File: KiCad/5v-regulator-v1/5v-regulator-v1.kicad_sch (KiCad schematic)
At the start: 43 parts, among them J1 Screw_Terminal_01x02, J2 USB-A1SSW6, J3 USB-A1SSW6, J4 USB-A1SSW6, J5 USB-A1SSW6, J6 Screw_Terminal_01x04, Q1 Q_Dual_NMOS_S1G1D2S2G2D1, SW1 SW_SPST, SW2 SW_SPST, U1 TPS51386RJNR, U2 INA219AIDR, U3 INA219AIDR

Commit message: Blaine review
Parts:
- added J7: Conn_01x04_Pin, Connector_PinHeader_2.54mm:PinHeader_1x04_P2.54mm_Vertical, symbol Connector:Conn_01x04_Pin
- added R11, R12: 10K, Resistor_SMD:R_0805_2012Metric_Pad1.20x1.40mm_HandSolder, symbol Device:R
- J2, J3, J4, J5: footprint Vertical USB:ONSHORE_USB-A1SSW6 -> Connector_USB:USB_A_Wuerth_614004134726_Horizontal; symbol Vertical USB-A:USB-A1SSW6 -> Connector:USB_A
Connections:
- net GND: now also J2.5 (Shield), J3.5 (Shield), J4.5 (Shield), J5.5 (Shield), J6.2 (Pin_2), J7.2 (Pin_2); no longer J2.S1 (SHIELD), J2.S2 (SHIELD__1), J2.S3 (SHIELD__2), J2.S4 (SHIELD__3), J3.S1 (SHIELD), J3.S2 (SHIELD__1), J3.S3 (SHIELD__2), J3.S4 (SHIELD__3), J4.S1 (SHIELD), J4.S2 (SHIELD__1), J4.S3 (SHIELD__2), J4.S4 (SHIELD__3), J5.S1 (SHIELD), J5.S2 (SHIELD__1), J5.S3 (SHIELD__2), J5.S4 (SHIELD__3), J6.3 (Pin_3)
- net VBATT: now also Q1.5 (G), R7.1; no longer U2.8 (VIN+)
- net VIN: no longer U2.7 (VIN-)
- net VOUT: no longer U3.8 (VIN+)
- net VOUT2: now also J6.3 (Pin_3), J7.1 (Pin_1), R11.1, R12.1; no longer J6.2 (Pin_2), U3.7 (VIN-)
- net at U2.2 (A0), U2.3 (SDA), U3.3 (SDA): now also J7.3 (Pin_3), R11.2
- net at U2.4 (SCL), U3.2 (A0), U3.4 (SCL): now also J7.4 (Pin_4), R12.2

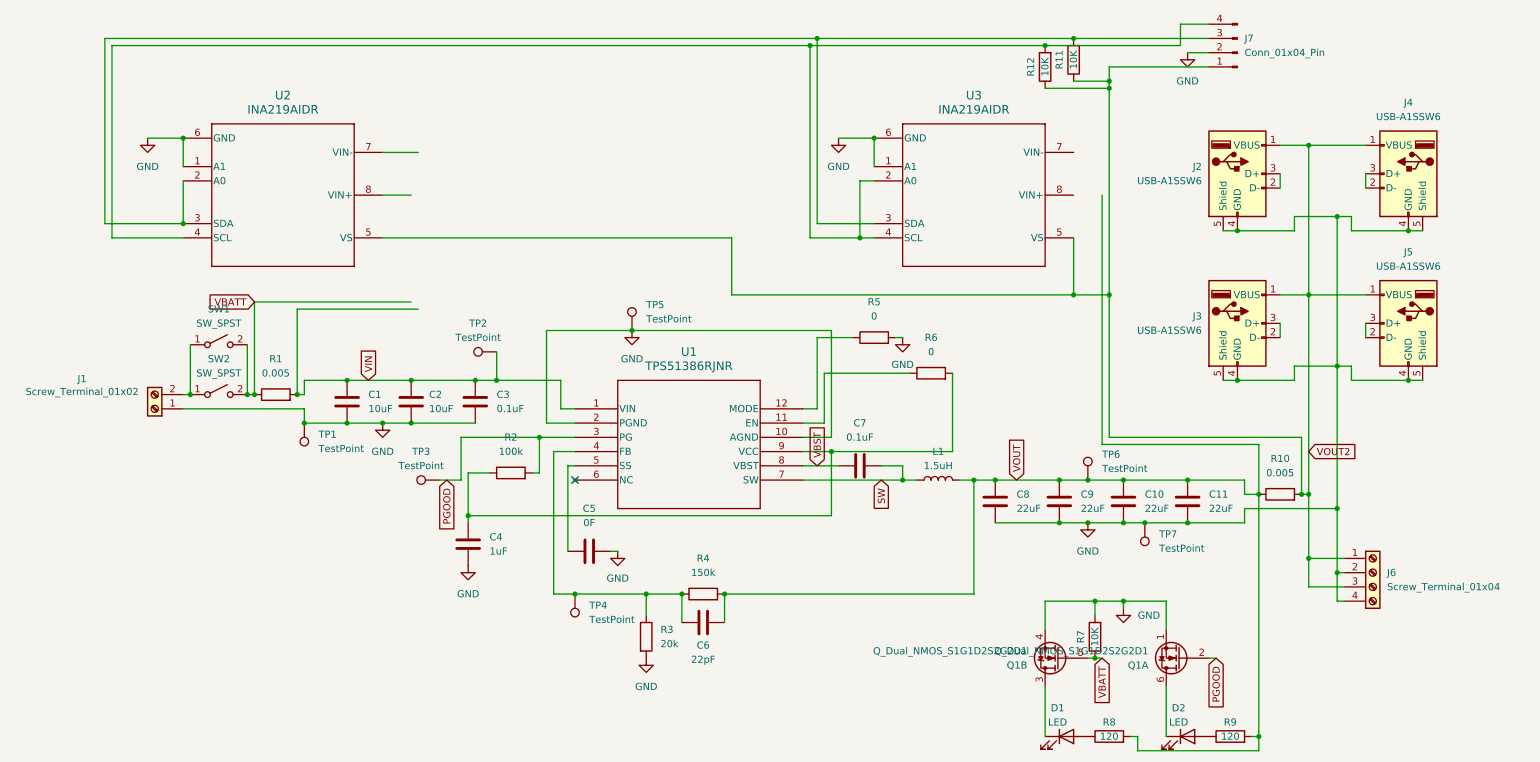
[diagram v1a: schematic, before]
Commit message: Updated 5V reg and added battery meter
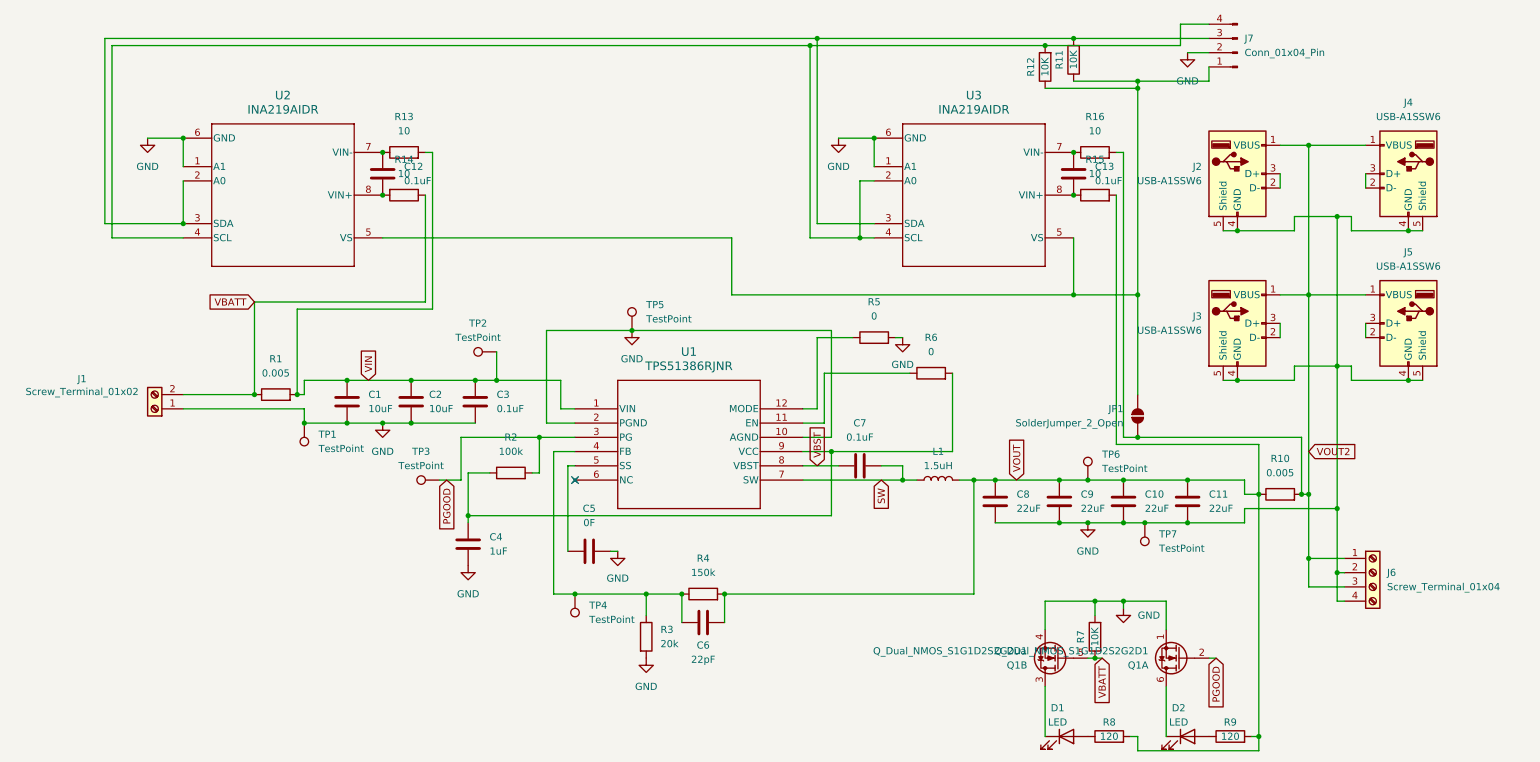
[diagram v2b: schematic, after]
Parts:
- removed SW1: SW_SPST, Connector_PinHeader_2.54mm:PinHeader_1x02_P2.54mm_Vertical, symbol Switch:SW_SPST
- removed SW2: SW_SPST, symbol Switch:SW_SPST
- added C12, C13: 0.1uF, Capacitor_SMD:C_1206_3216Metric_Pad1.33x1.80mm_HandSolder, symbol Device:C
- added JP1: SolderJumper_2_Open, Jumper:SolderJumper-2_P1.3mm_Open_TrianglePad1.0x1.5mm, symbol Jumper:SolderJumper_2_Open
- added R13, R14, R15, R16: 10, Resistor_SMD:R_1206_3216Metric_Pad1.30x1.75mm_HandSolder, symbol Device:R
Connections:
- net VBATT: now also J1.2 (Pin_2), R14.1
- net VIN: now also R13.2
- net VOUT: now also R15.2
- net VOUT2: now also JP1.1 (A), R16.2; no longer J7.1 (Pin_1), R11.1, R12.1, U2.5 (VS), U3.5 (VS)
- net at U2.7 (VIN-): now also C12.1, R13.1
- net at U2.8 (VIN+): now also C12.2, R14.2
- net at U3.7 (VIN-): now also C13.1, R16.1
- net at U3.8 (VIN+): now also C13.2, R15.1
- new net: J7.1 (Pin_1), JP1.2 (B), R11.1, R12.1, U2.5 (VS), U3.5 (VS)

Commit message: Sent to production!
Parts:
- added JP2: Jumper_2_Bridged, TPS51386:usb_symbol, symbol Jumper:Jumper_2_Bridged
- C5, R5, R6: now not fitted
- L1: footprint Wurth_Inductor:IND_WE-LHMI_8030_WRE -> TPS51386:L_Panasonic_ETQP4M---KVK
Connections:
- net at J7.1 (Pin_1), JP1.2 (B), R11.1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: now also JP2.1 (A)
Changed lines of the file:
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@@
 	)
 	(junction
+		(at 130.81 62.23)
+		(diameter 0)
+		(color 0 0 0 0)
+	)
+	(junction
 		(at 72.39 95.25)
 		(diameter 0)
@@
 	(wire
 		(pts
-			(xy 261.62 87.63) (xy 264.16 87.63)
+			(xy 130.81 72.39) (xy 201.93 72.39)
 		)
 		(stroke
@@
 	(wire
 		(pts
-			(xy 241.3 58.42) (xy 248.92 58.42)
+			(xy 261.62 87.63) (xy 264.16 87.63)
 		)
 		(stroke
@@
 	(wire
 		(pts
-			(xy 238.76 72.39) (xy 243.84 72.39)
+			(xy 241.3 58.42) (xy 248.92 58.42)
 		)
 		(stroke
@@
 	(wire
 		(pts
-			(xy 232.41 107.95) (xy 232.41 105.41)
+			(xy 238.76 72.39) (xy 243.84 72.39)
 		)
 		(stroke
@@
 	(wire
 		(pts
-			(xy 238.76 45.72) (xy 243.84 45.72)
+			(xy 232.41 107.95) (xy 232.41 105.41)
 		)
 		(stroke
@@
 	(wire
 		(pts
-			(xy 201.93 34.29) (xy 213.36 34.29)
+			(xy 238.76 45.72) (xy 243.84 45.72)
 		)
 		(stroke
@@
 	(wire
 		(pts
-			(xy 105.41 104.14) (xy 106.68 104.14)
+			(xy 201.93 34.29) (xy 213.36 34.29)
 		)
 		(stroke
@@
 	(wire
 		(pts
-			(xy 78.74 62.23) (xy 140.97 62.23)
+			(xy 105.41 104.14) (xy 106.68 104.14)
 		)
 		(stroke
@@
 	(wire
 		(pts
-			(xy 140.97 72.39) (xy 201.93 72.39)
+			(xy 130.81 72.39) (xy 130.81 62.23)
 		)
 		(stroke
@@
 	(wire
 		(pts
+			(xy 78.74 62.23) (xy 130.81 62.23)
+		)
+		(stroke
+			(width 0)
+			(type default)
+		)
+	)
+	(wire
+		(pts
 			(xy 201.93 62.23) (xy 201.93 72.39)
 		)
@@
 	(wire
 		(pts
-			(xy 140.97 62.23) (xy 140.97 72.39)
-		)
-		(stroke
-			(width 0)
-			(type default)
-		)
-	)
-	(wire
-		(pts
 			(xy 184.15 105.41) (xy 187.96 105.41)
 		)
@@
 	(global_label "VOUT2"
 		(shape input)
-		(at 243.84 100.33 0)
+		(at 243.84 92.71 180)
 		(fields_autoplaced yes)
 		(effects
@@
 				(size 1.27 1.27)
 			)
-			(justify left)
+			(justify right)
 		)
 		(property "Intersheetrefs" "${INTERSHEET_REFS}"
-			(at 252.7519 100.33 0)
+			(at 234.9281 92.71 0)
 			(effects
 				(font
 					(size 1.27 1.27)
 				)
-				(justify left)
+				(justify right)
 				(hide yes)
 			)
@@
 		(in_bom yes)
 		(on_board yes)
-		(dnp no)
+		(dnp yes)
 		(fields_autoplaced yes)
 		(property "Reference" "R5"
@@
 		(in_bom yes)
 		(on_board yes)
-		(dnp no)
+		(dnp yes)
 		(fields_autoplaced yes)
 		(property "Reference" "R6"
@@
 		(in_bom yes)
 		(on_board yes)
-		(dnp no)
+		(dnp yes)
 		(fields_autoplaced yes)
 		(property "Reference" "C5"
@@
 	)
 	(symbol
+		(lib_id "Jumper:Jumper_2_Bridged")
+		(at 135.89 62.23 0)
+		(unit 1)
+		(exclude_from_sim yes)
+		(in_bom yes)
+		(on_board yes)
+		(dnp no)
+		(fields_autoplaced yes)
+		(property "Reference" "JP2"
+			(at 135.89 57.15 0)
+			(effects
+				(font
+					(size 1.27 1.27)
+				)
+			)
+		)
+		(property "Value" "Jumper_2_Bridged"
+			(at 135.89 59.69 0)
+			(effects
+				(font
+					(size 1.27 1.27)
+				)
+			)
+		)
+		(property "Footprint" "TPS51386:usb_symbol"
+			(at 135.89 62.23 0)
+			(effects
+				(font
+					(size 1.27 1.27)
+				)
+				(hide yes)
+			)
+		)
+		(property "Datasheet" "~"
+			(at 135.89 62.23 0)
+			(effects
+				(font
+					(size 1.27 1.27)
+				)
+				(hide yes)
+			)
+		)
+		(property "Description" "Jumper, 2-pole, closed/bridged"
+			(at 135.89 62.23 0)
+			(effects
+				(font
+					(size 1.27 1.27)
+				)
+				(hide yes)
+			)
+		)
+		(pin "2"
+		)
+		(pin "1"
+		)
+		(instances
+			(project "5v-regulator-v1"
+				(path "/4305ae50-7d96-42de-9eb2-54fda8fc6884"
+					(reference "JP2")
+					(unit 1)
+				)
+			)
+		)
+	)
+	(symbol
 		(lib_id "Device:C")
 		(at 222.25 109.22 0)
@@
 			)
 		)
-		(property "Footprint" "Wurth_Inductor:IND_WE-LHMI_8030_WRE"
+		(property "Footprint" "TPS51386:L_Panasonic_ETQP4M---KVK"
 			(at 177.8 105.41 0)
 			(effects

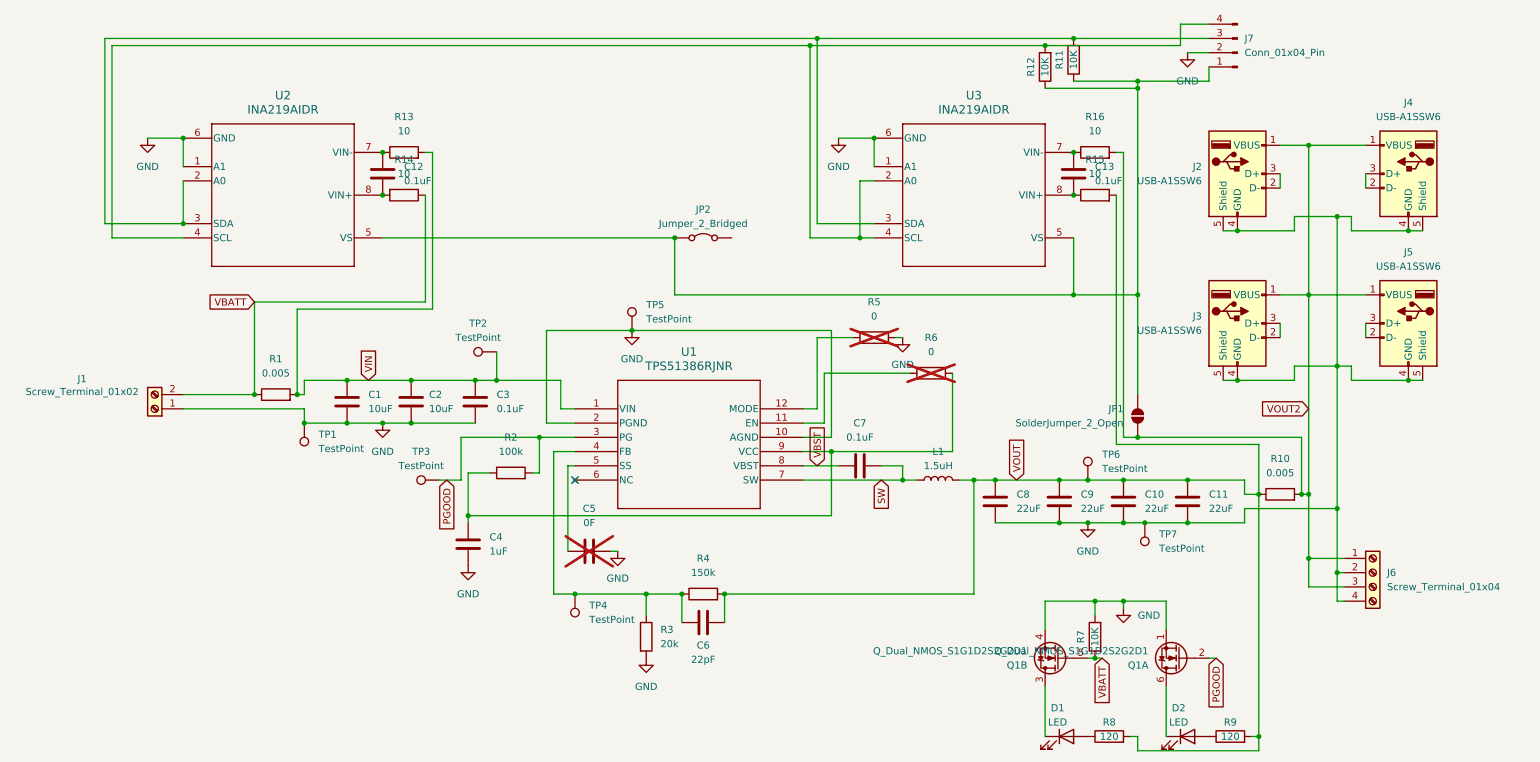
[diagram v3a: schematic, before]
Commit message: Fixed errors (missing enable & overlapping trace)
I should really RTFM and run the DRC...
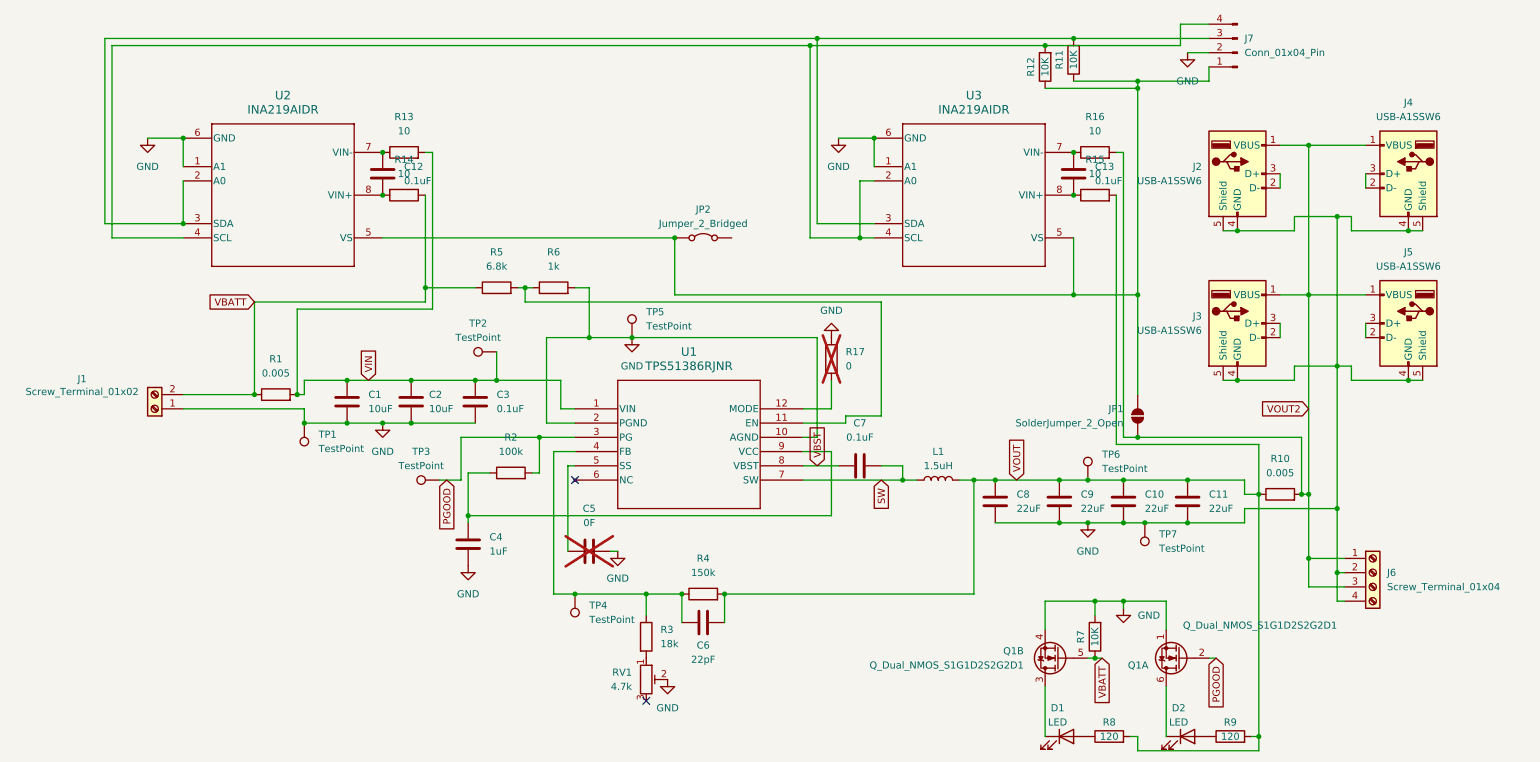
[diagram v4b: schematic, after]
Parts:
- added R5: 6.8k, Resistor_SMD:R_0805_2012Metric_Pad1.20x1.40mm_HandSolder, symbol Device:R
- added RV1: 4.7k, Potentiometer_SMD:Potentiometer_Bourns_TC33X_Vertical, symbol Device:R_Potentiometer_Trim
- R3: value 20k -> 18k
- R6: value 0 -> 1k; footprint Resistor_SMD:R_1206_3216Metric_Pad1.30x1.75mm_HandSolder -> Resistor_SMD:R_0805_2012Metric_Pad1.20x1.40mm_HandSolder; now fitted
- renumbered R5 to R17
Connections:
- net GND: now also R6.2, RV1.2; no longer R3.2
- net VBATT: now also R5.1
- net at C4.1, R2.1, U1.9 (VCC): no longer R6.2
- net at R6.1, U1.11 (EN): now also R5.2
- new net: R3.2, RV1.1
- no-connect marks 1 -> 2
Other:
- moved on the sheet: R17, TP5
